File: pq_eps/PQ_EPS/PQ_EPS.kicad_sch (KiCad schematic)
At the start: 86 parts, among them IC1 DS2782E+, IC2 ISL9120IRTNZ, J1 SLW-110-01-T-S, J2 SLW-110-01-T-S, J3 SLW-110-01-T-S, J4 SLW-110-01-T-S, Q1 SIR424DP, U1 SPV1040TTR, U2 SPV1040TTR, U3 SPV1040TTR, U4 LTC4040EUFD#PBF

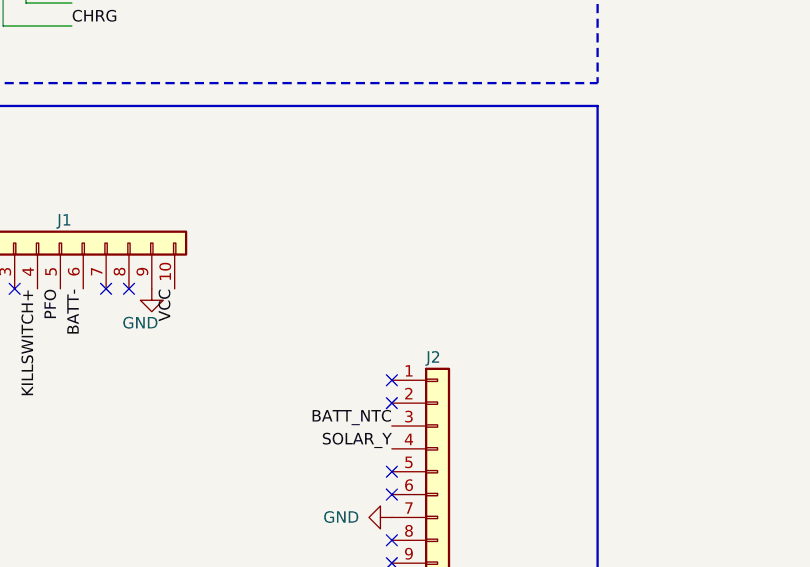
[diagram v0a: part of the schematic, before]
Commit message: Added MPPT input pin for testing on board of the EGSE of the PQ nominal operation: Battery and MPPT input both in use
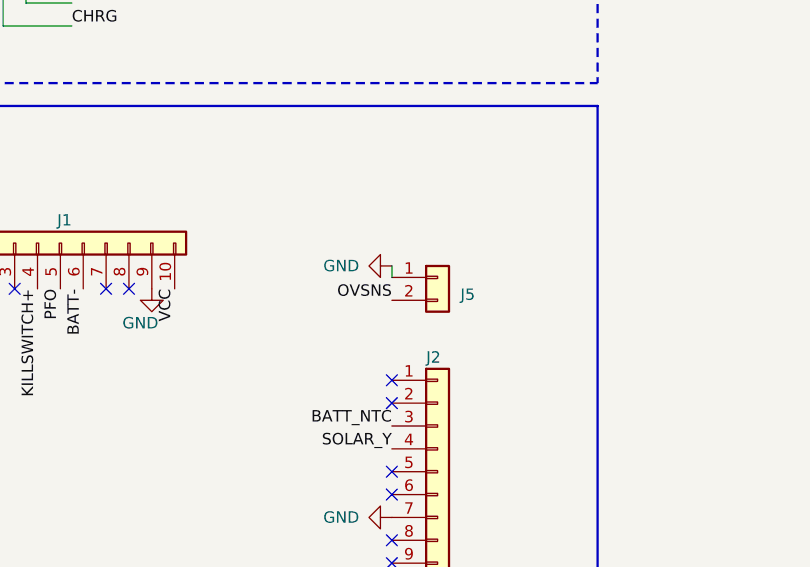
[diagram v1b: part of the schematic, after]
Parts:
- added J5: ~, -nsl_connector:CES-102-02, symbol -nsl_connector:CES-102-02
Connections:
- net GND: now also J5.1
- net OVSNS: now also J5.2
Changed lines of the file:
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@@
     (stroke (width 0.254) (type default))
   )
+  (wire (pts (xy 323.85 154.94) (xy 323.85 156.21))
+    (stroke (width 0) (type default))
+  )
   (wire (pts (xy 334.01 107.95) (xy 318.77 107.95))
     (stroke (width 0.254) (type default))
@@
     (effects (font (size 1.27 1.27)) (justify left bottom))
   )
+  (label "OVSNS" (at 323.85 158.75 180) (fields_autoplaced)
+    (effects (font (size 1.27 1.27)) (justify right bottom))
+  )
   (symbol (lib_id "power:GND") (at 125.73 111.76 0) (unit 1)
     (in_bom yes) (on_board yes) (dnp no) (fields_autoplaced)
@@
     )
   )
+  (symbol (lib_id "-nsl_connector:CES-102-02") (at 328.93 157.48 0) (unit 1)
+    (in_bom yes) (on_board yes) (dnp no) (fields_autoplaced)
+    (property "Reference" "J5" (at 331.47 158.115 0)
+      (effects (font (size 1.27 1.27)) (justify left))
+    )
+    (property "Value" "~" (at 328.93 157.48 0)
+      (effects (font (size 1.27 1.27)))
+    )
+    (property "Footprint" "-nsl_connector:CES-102-02" (at 327.66 161.29 0)
+      (effects (font (size 1.27 1.27)) hide)
+    )
+    (property "Datasheet" "" (at 328.93 157.48 0)
+      (effects (font (size 1.27 1.27)) hide)
+    )
+    (pin "1")
+    (pin "2")
+    (instances
+      (project "PQ_EPS"
+        (path "/369ed984-4bc0-4563-9a96-3c71b74c6c81"
+          (reference "J5") (unit 1)
+        )
+      )
+    )
+  )
   (symbol (lib_id "PCB-EPS-altium-import:1_1.5u") (at 83.82 106.68 0) (unit 1)
     (in_bom yes) (on_board yes) (dnp no) (fields_autoplaced)
@@
         )
       )
+    )
+  )
+  (symbol (lib_id "power:GND") (at 323.85 154.94 270) (unit 1)
+    (in_bom yes) (on_board yes) (dnp no)
+    (property "Reference" "#PWR06" (at 323.85 154.94 0)
+      (effects (font (size 1.27 1.27)) hide)
+    )
+    (property "Value" "GND" (at 316.23 154.94 90)
+      (effects (font (size 1.27 1.27)) (justify left))
+    )
+    (property "Footprint" "" (at 323.85 154.94 0)
+      (effects (font (size 1.27 1.27)) hide)
+    )
+    (property "Datasheet" "" (at 323.85 154.94 0)
+      (effects (font (size 1.27 1.27)) hide)
+    )
+    (pin "1")
+    (instances
+      (project "PQ_EPS"
+        (path "/369ed984-4bc0-4563-9a96-3c71b74c6c81"
+          (reference "#PWR06") (unit 1)
+        )
+      )

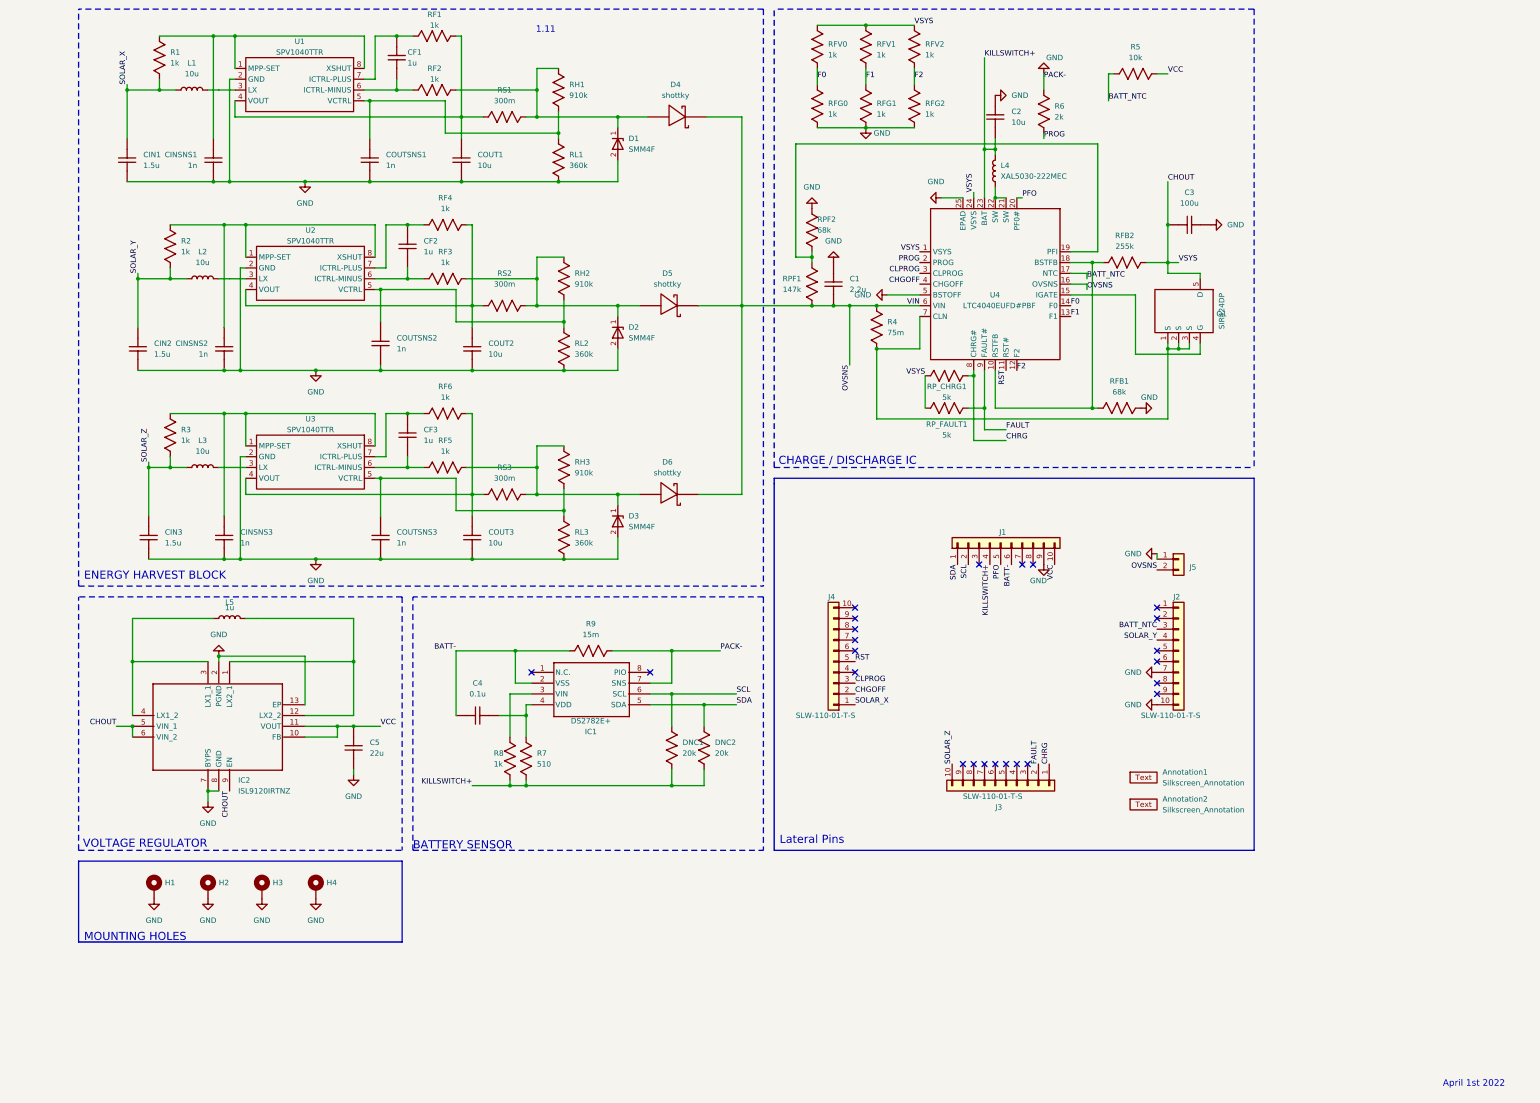
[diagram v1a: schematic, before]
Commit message: Altium symbol imports fix, rotated J3, updated track widths for power lines, solved courtyard conflicts, DRC
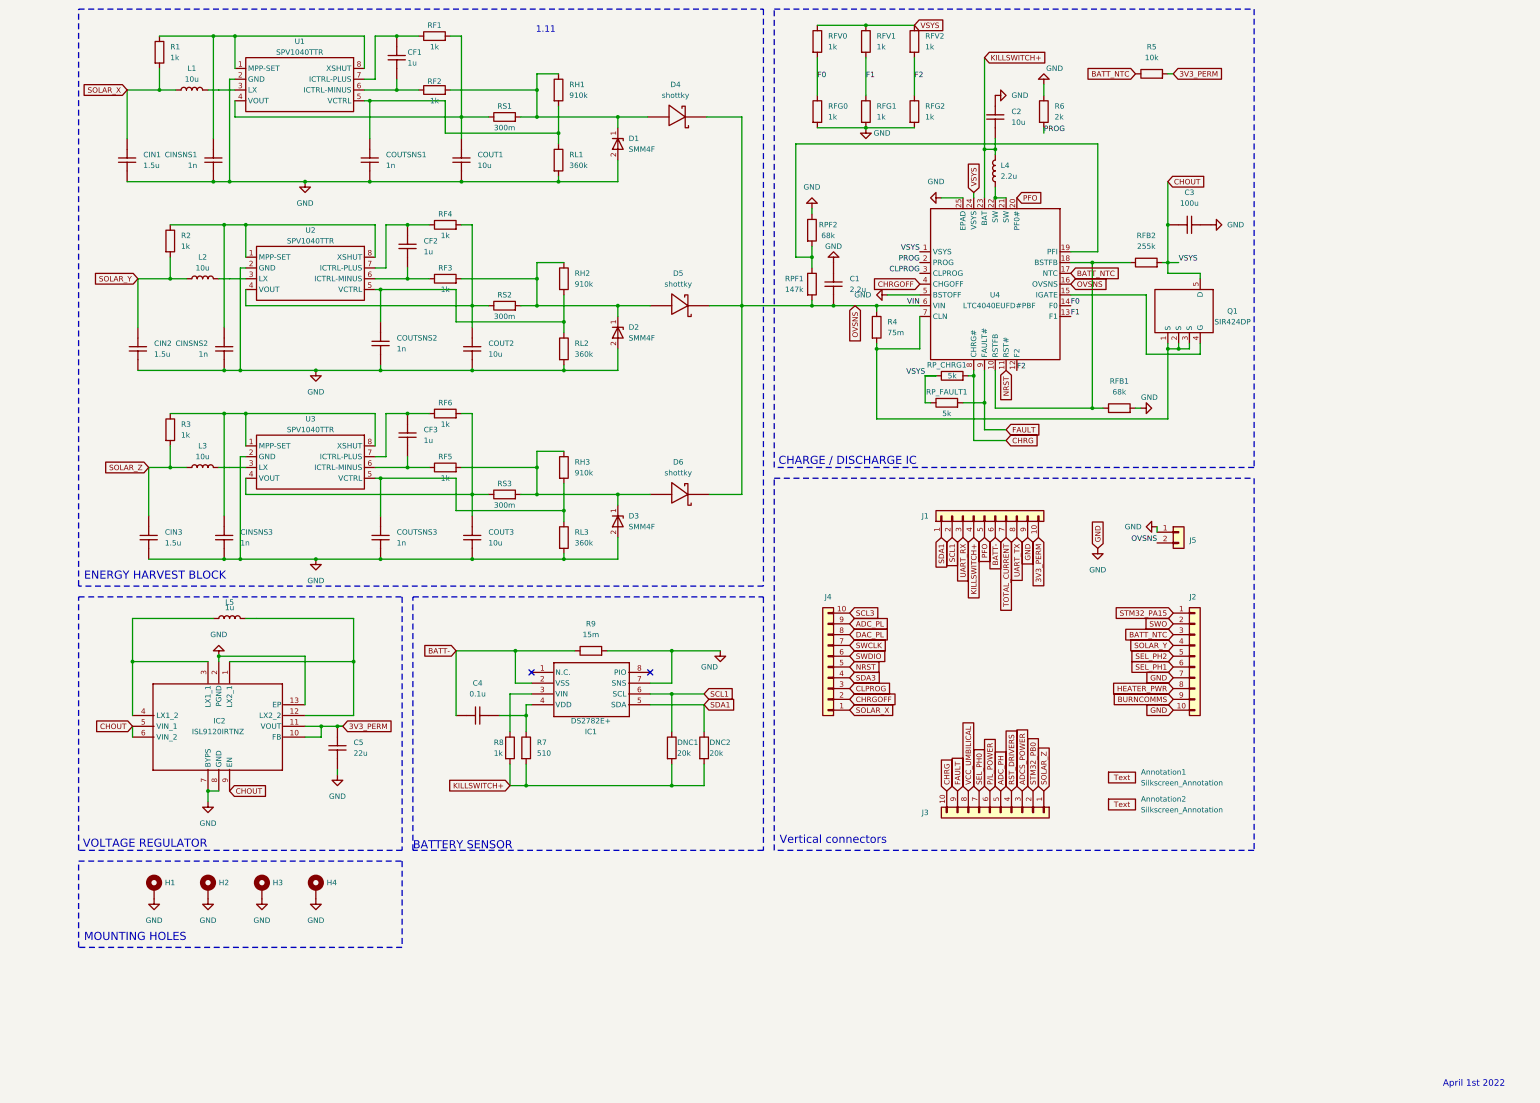
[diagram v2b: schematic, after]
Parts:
- removed J1, J2, J3, J4: SLW-110-01-T-S, SLW-110-01, symbol connector-nsl:SLW-110-01
- removed R1, R2, R3, R8: 1k, Resistor_SMD:R_0603_1608Metric, symbol PCB-EPS-altium-import:1_1k
- removed R5: 10k, Resistor_SMD:R_0603_1608Metric, symbol PCB-EPS-altium-import:0_255k
- removed R6: 2k, Resistor_SMD:R_0603_1608Metric, symbol PCB-EPS-altium-import:1_14k
- removed R7: 510, Resistor_SMD:R_0603_1608Metric, symbol PCB-EPS-altium-import:1_510
- removed R9: 15m, Resistor_SMD:R_0603_1608Metric, symbol PCB-EPS-altium-import:2_15m
- added J1, J2, J3, J4: CES-110-02-L-S, connector-nsl:SLW-110-01, symbol Connector_Generic:Conn_01x10
- added R1, R2, R3, R8: 1k, Resistor_SMD:R_0603_1608Metric, symbol Device:R
- added R5: 10k, Resistor_SMD:R_0603_1608Metric, symbol Device:R
- added R6: 2k, Resistor_SMD:R_0603_1608Metric, symbol Device:R
- added R7: 510, Resistor_SMD:R_0603_1608Metric, symbol Device:R
- added R9: 15m, Resistor_SMD:R_0603_1608Metric, symbol Device:R
- Annotation1: footprint -nsl_symbols:Bridgemaker -> symbols-nsl:Bridgemaker
- Annotation2: footprint -nsl_symbols:NakNak -> symbols-nsl:NakNak
- D1, D2, D3: footprint DO-222AA-2 -> passive-nsl:SMM4F15ATR
- D4, D5, D6: footprint SOD-128-2 -> passive-nsl:RBS1LAM40ATR_Schottky
- DNC1, DNC2: symbol PCB-EPS-altium-import:1_20k -> Device:R
- IC2: footprint TQFN-12 -> power-nsl:ISL9120IRTNZ
- J5: footprint -nsl_connector:CES-102-02 -> connector-nsl:CES-102-02
- L4: value XAL5030-222MEC -> 2.2u; footprint 2221 -> passive-nsl:XAL5030222MEC
- Q1: footprint PowerPAK-SO-8 -> power-nsl:SIR424DP
- R4: symbol PCB-EPS-altium-import:1_75m -> Device:R
- RF1, RF2, RF3, RF4, RF5, RF6: symbol PCB-EPS-altium-import:0_1k -> Device:R
- RFB1: symbol PCB-EPS-altium-import:0_68k -> Device:R
- RFB2: symbol PCB-EPS-altium-import:0_255k -> Device:R
- RFG0, RFG1, RFG2, RFV0, RFV1, RFV2: symbol PCB-EPS-altium-import:1_1k -> Device:R
- RH1, RH2, RH3: symbol PCB-EPS-altium-import:1_910k -> Device:R
- RL1, RL2, RL3: symbol PCB-EPS-altium-import:1_360k -> Device:R
- RPF1: symbol PCB-EPS-altium-import:1_147k -> Device:R
- RPF2: symbol PCB-EPS-altium-import:1_68k -> Device:R
- RP_CHRG1, RP_FAULT1: symbol PCB-EPS-altium-import:2_5k -> Device:R
- RS1, RS2, RS3: symbol PCB-EPS-altium-import:0_300m -> Device:R
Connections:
- net BATT-: now also J1.6 (Pin_6), R9.1
- net BATT_NTC: now also J2.3 (Pin_3), R5.1
- net CHOUT: now also RFV0.1, RFV1.1, RFV2.1, RP_CHRG1.1, RP_FAULT1.1; no longer RFV0.2, RFV1.2, RFV2.2, RP_CHRG1.2, RP_FAULT1.2
- net CHRG: now also RP_CHRG1.2, J3.10 (Pin_10); no longer RP_CHRG1.1
- net CLPROG: now also J4.3 (Pin_3)
- net F0: now also RFG0.1, RFV0.2; no longer RFG0.2, RFV0.1
- net F1: now also RFG1.1, RFV1.2; no longer RFG1.2, RFV1.1
- net F2: now also RFG2.1, RFV2.2; no longer RFG2.2, RFV2.1
- net FAULT: now also RP_FAULT1.2, J3.9 (Pin_9); no longer RP_FAULT1.1
- net GND: now also RFG0.2, RFG1.2, RFG2.2, RL1.2, RL2.2, RL3.2, RPF2.1, J1.9 (Pin_9), J2.10 (Pin_10), J2.7 (Pin_7), R6.1, R9.2; no longer RFG0.1, RFG1.1, RFG2.1, RL1.1, RL2.1, RL3.1, RPF2.2
- net KILLSWITCH+: now also DNC1.2, DNC2.2, J1.4 (Pin_4), R7.2, R8.2; no longer DNC1.1, DNC2.1
- net OVSNS: now also R4.1, RPF1.2; no longer R4.2, RPF1.1
- net PFO: now also J1.5 (Pin_5)
- net PROG: now also R6.2
- net SOLAR_X: now also J4.1 (Pin_1), R1.2
- net SOLAR_Y: now also J2.4 (Pin_4), R2.2
- net SOLAR_Z: now also J3.1 (Pin_1), R3.2
- net at IC1.3 (VIN): now also R8.1
- net at COUTSNS2.2, U2.5 (VCTRL): now also RH2.2, RL2.1; no longer RH2.1, RL2.2
- net at D2.1, D5.2, RF3.2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: now also RH2.1; no longer RH2.2
- net at CINSNS2.2, U2.1 (MPP-SET), U2.8 (XSHUT): now also R2.1
- net at COUTSNS1.2, U1.5 (VCTRL): now also RH1.2, RL1.1; no longer RH1.1, RL1.2
- net at D1.1, D4.2, RF2.2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: now also RH1.1; no longer RH1.2
- net at Q1.1 (S), Q1.2 (S), Q1.3 (S)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: now also R4.2; no longer R4.1
- net at COUTSNS3.2, U3.5 (VCTRL): now also RH3.2, RL3.1; no longer RH3.1, RL3.2
- net at D3.1, D6.2, RF5.2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: now also RH3.1; no longer RH3.2
- net at CINSNS1.2, U1.1 (MPP-SET), U1.8 (XSHUT): now also R1.1
- net at CINSNS3.2, U3.1 (MPP-SET), U3.8 (XSHUT): now also R3.1
- net at C4.1, IC1.4 (VDD): now also R7.1
- net CHGOFF renamed CHRGOFF
- net CHRGOFF: now also J4.2 (Pin_2)
- net RST renamed NRST
- net NRST: now also J4.5 (Pin_5)
- net SCL renamed SCL1
- net SCL1: now also DNC1.1, J1.2 (Pin_2); no longer DNC1.2
- net SDA renamed SDA1
- net SDA1: now also DNC2.1, J1.1 (Pin_1); no longer DNC2.2
- net VCC renamed 3V3_PERM
- net 3V3_PERM: now also J1.10 (Pin_10), R5.2
- new net: RPF1.1, RPF2.2, U4.19 (PFI)
- new net ADCS_POWER: J3.3 (Pin_3)
- new net ADC_PH: J3.5 (Pin_5)
- new net ADC_PL: J4.9 (Pin_9)
- new net BURNCOMMS: J2.9 (Pin_9)
- new net DAC_PL: J4.8 (Pin_8)
- new net HEATER_PWR: J2.8 (Pin_8)
- new net P/L_POWER: J3.6 (Pin_6)
- new net RST_DRIVERS: J3.4 (Pin_4)
- new net SCL3: J4.10 (Pin_10)
- new net SDA3: J4.4 (Pin_4)
- new net SEL_PH0: J3.7 (Pin_7)
- new net SEL_PH1: J2.6 (Pin_6)
- new net SEL_PH2: J2.5 (Pin_5)
- new net STM32_PA15: J2.1 (Pin_1)
- new net STM32_PB0: J3.2 (Pin_2)
- new net SWCLK: J4.7 (Pin_7)
- new net SWDIO: J4.6 (Pin_6)
- new net SWO: J2.2 (Pin_2)
- new net TOTAL_CURRENT: J1.7 (Pin_7)
- new net UART_RX: J1.3 (Pin_3)
- new net UART_TX: J1.8 (Pin_8)
- new net VCC_UMBILICAL: J3.8 (Pin_8)
- no-connect marks 24 -> 2
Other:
- note added: "Vertical connectors"
- note removed: "Lateral Pins"
- moved on the sheet: Annotation1, Annotation2, C5, D5, D6, J5
